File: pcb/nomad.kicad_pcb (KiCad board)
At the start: 2 copper layers, 61 x 142 mm, 65 parts, among them J1 USB_C_Receptacle_USB2.0_16P, J2 Conn_01x08_Pin, J3 Conn_Coaxial, J4 Conn_Coaxial, J5 Conn_01x02_Pin, Q2 2N7002, SW1 UP, SW2 DOWN, SW3 RIGHT, SW4 LEFT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

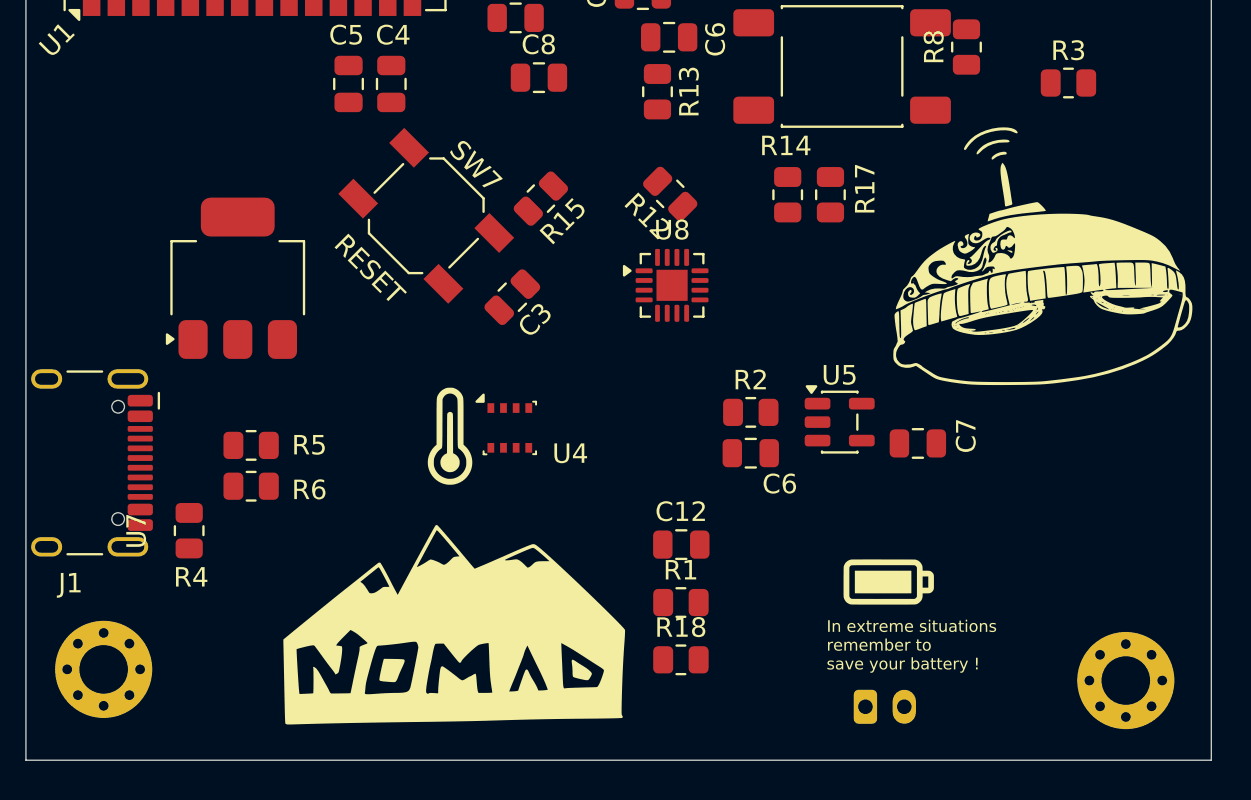
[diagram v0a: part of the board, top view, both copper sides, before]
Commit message: Updating PCB: Adding Buck boost converter, battery protection and other fixes.
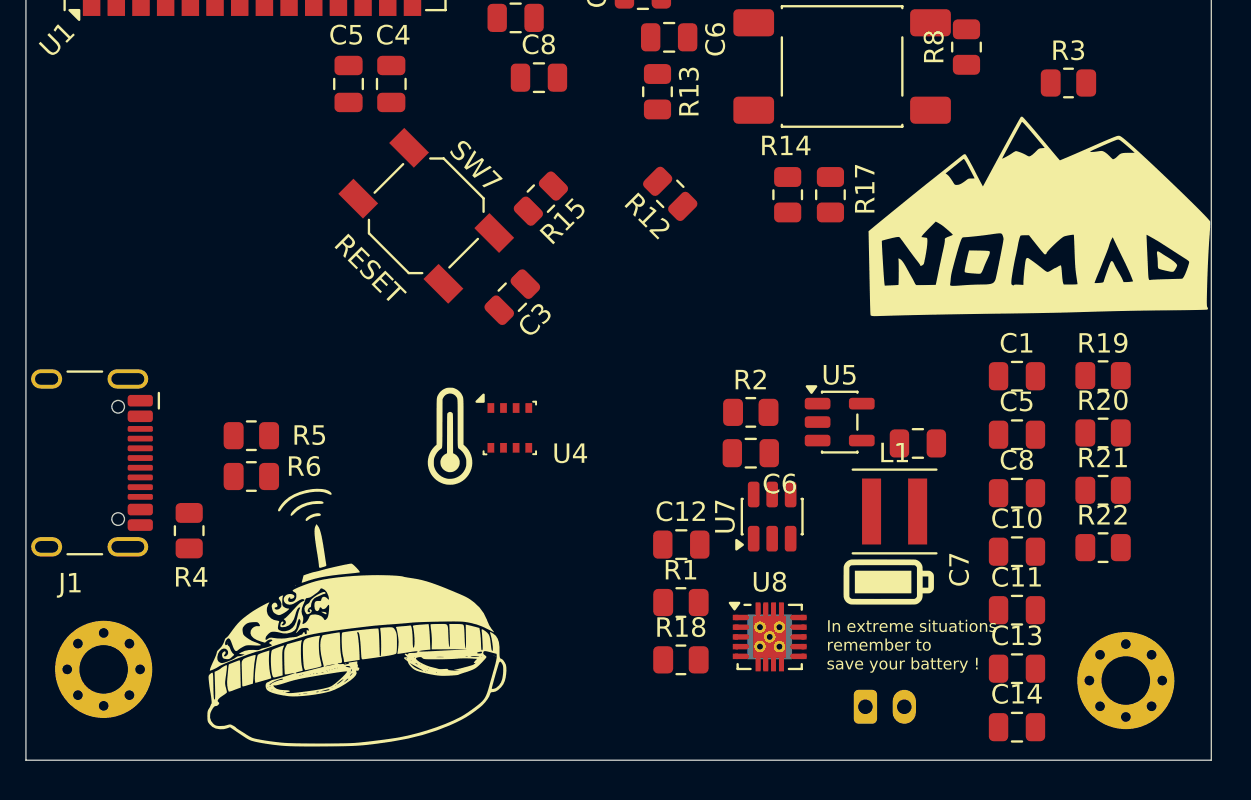
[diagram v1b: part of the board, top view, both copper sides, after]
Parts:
- added C1: C, Capacitor_SMD:C_0805_2012Metric, F.Cu at (151.0, 142.2)
- added C10: C, Capacitor_SMD:C_0805_2012Metric, F.Cu at (151.0, 151.3)
- added C11: C, Capacitor_SMD:C_0805_2012Metric, F.Cu at (151.0, 154.3)
- added C13: 10uF, Capacitor_SMD:C_0805_2012Metric, F.Cu at (151.0, 157.3)
- added C14: 66uF, Capacitor_SMD:C_0805_2012Metric, F.Cu at (151.0, 160.3)
- added C5: 22uF, Capacitor_SMD:C_0805_2012Metric, F.Cu at (151.0, 145.2)
- added C8: 0.1uF, Capacitor_SMD:C_0805_2012Metric, F.Cu at (151.0, 148.3)
- added L1: 1uH, Inductor_SMD:L_Coilcraft_XxL4020, F.Cu at (144.7, 149.2)
- added R19: 100R, Resistor_SMD:R_0805_2012Metric, F.Cu at (155.4, 142.2)
- added R20: 560k, Resistor_SMD:R_0805_2012Metric, F.Cu at (155.4, 145.2)
- added R21: 1M, Resistor_SMD:R_0805_2012Metric, F.Cu at (155.4, 148.1)
- added R22: 100k, Resistor_SMD:R_0805_2012Metric, F.Cu at (155.4, 151.1)
- U7: value AMS1117-3.3 -> DW01A; footprint Package_TO_SOT_SMD:SOT-223-3_TabPin2 -> Package_TO_SOT_SMD:SOT-23-6
- U8: value BQ24075RGT -> TPS63060; footprint Package_DFN_QFN:VQFN-16-1EP_3x3mm_P0.5mm_EP1.6x1.6mm -> Package_SON:Texas_S-PWSON-N10_ThermalVias
- moved G*** 39.9 mm to (131.2, 202.3)
- moved G*** 36.7 mm to (152.2, 134.1)
- moved U7 30.1 mm to (138.4, 149.5)
- moved U8 18.8 mm to (138.3, 155.7)
- moved R5 0.50 mm to (111.6, 145.3)
- moved R6 0.50 mm to (111.6, 147.4)
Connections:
- C6 pad 1: Net-(J5-Pin_1) -> +BATT
- J2 pad 5: SDA -> MOSI
- J2 pad 6: SCL -> SCLK
- J5 pad 1: Net-(J5-Pin_1) -> +BATT
- J5 pad 2: GND -> -BATT
- U1 pad 18: unconnected-(U1-IO10-Pad18) -> CS
- U1 pad 19: unconnected-(U1-IO11-Pad19) -> MOSI
- U1 pad 20: unconnected-(U1-IO12-Pad20) -> SCLK
- U1 pad 25: unconnected-(U1-IO48-Pad25) -> M1
- U1 pad 31: unconnected-(U1-IO38-Pad31) -> M0
- U1 pad 38: unconnected-(U1-IO2-Pad38) -> BUTTON_INT
- U1 pad 39: unconnected-(U1-IO1-Pad39) -> FLASHLIGHT
- U1 pad 6: unconnected-(U1-IO6-Pad6) -> RES
- U1 pad 7: unconnected-(U1-IO7-Pad7) -> DC
- U5 pad 3: Net-(J5-Pin_1) -> +BATT
- U7 pad 1: GND -> unconnected-(U7-OD-Pad1)
- U7 pad 2: +3V3 -> unconnected-(U7-CS-Pad2)
- U7 pad 3: +5V -> unconnected-(U7-OC-Pad3)
- U8 pad 1: unconnected-(U8-TS-Pad1) -> Net-(U8-L1)
- U8 pad 10: Net-(U8-OUT-Pad10) -> Net-(U8-L2)
- U8 pad 11: Net-(U8-OUT-Pad10) -> GND
- U8 pad 2: Net-(U8-BAT-Pad2) -> +BATT
- U8 pad 3: Net-(U8-BAT-Pad2) -> +BATT
- U8 pad 4: unconnected-(U8-~{CE}-Pad4) -> GND
- U8 pad 5: unconnected-(U8-EN2-Pad5) -> Net-(U8-PG)
- U8 pad 6: unconnected-(U8-EN1-Pad6) -> Net-(U8-VAUX)
- U8 pad 7: unconnected-(U8-~{PGOOD}-Pad7) -> GND
- U8 pad 8: Net-(U8-VSS-Pad17) -> Net-(U8-FB)
- U8 pad 9: unconnected-(U8-~{CHG}-Pad9) -> Net-(U8-VOUT)
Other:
- board text added: "USB-C > charging IC > JST > MAX > Buck boost"

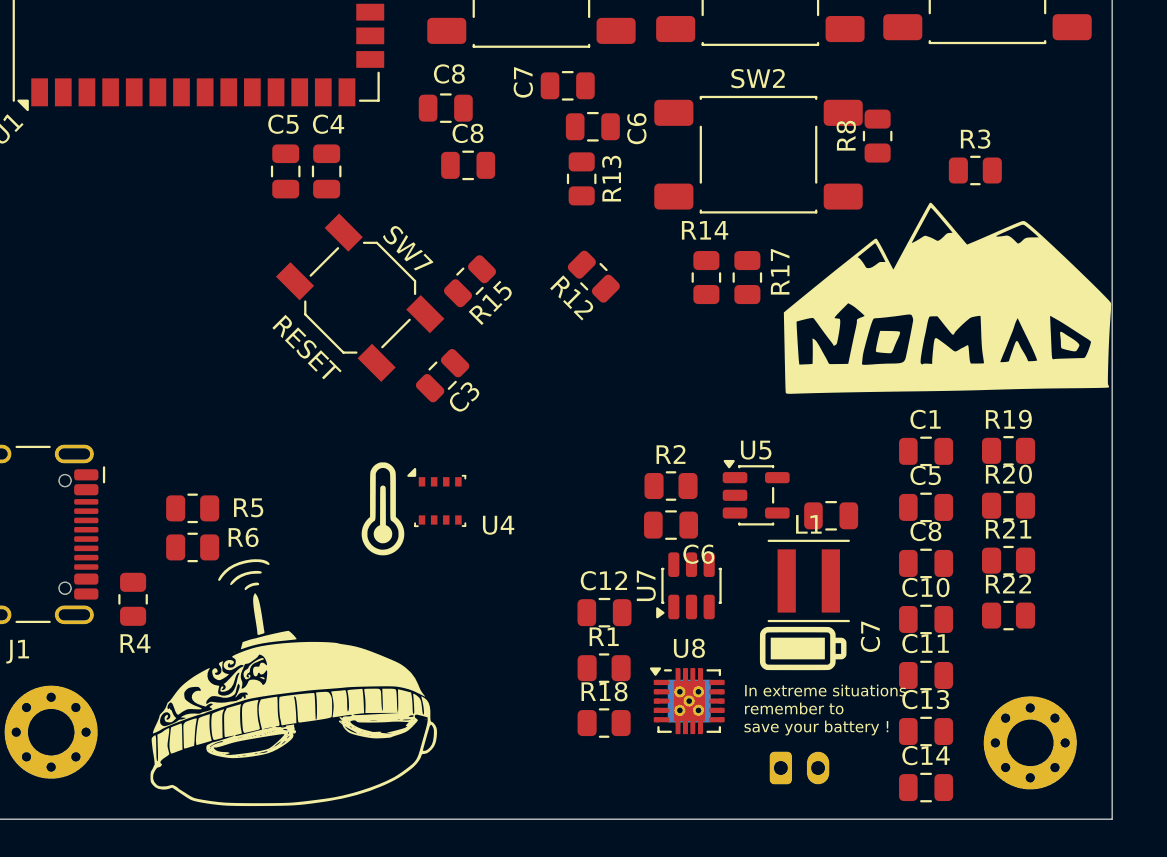
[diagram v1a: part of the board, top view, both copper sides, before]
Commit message: Updating PCB: Removing battery security and adding slide switch
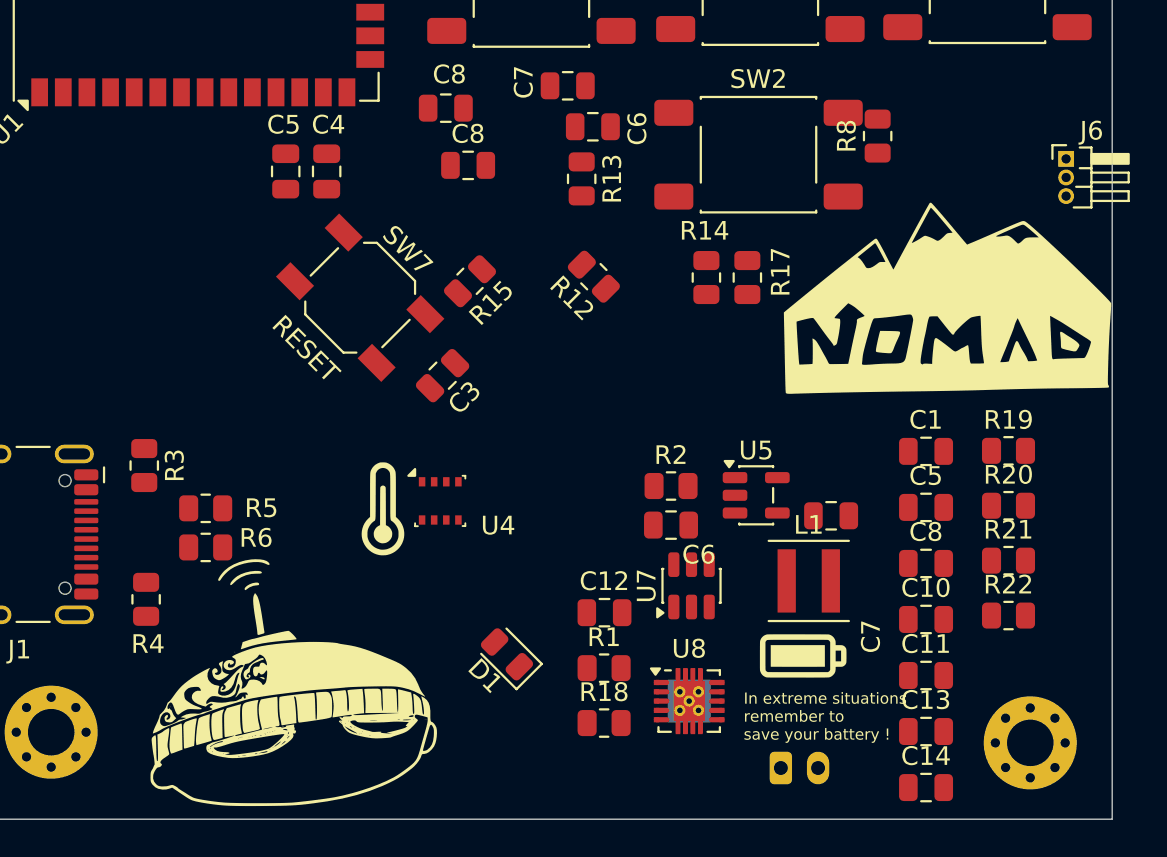
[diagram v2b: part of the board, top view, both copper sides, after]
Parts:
- added D1: LED, LED_SMD:LED_0805_2012Metric, F.Cu at (128.5, 153.1)
- added J6: Conn_01x03_Socket, Connector_PinHeader_1.00mm:PinHeader_1x03_P1.00mm_Horizontal, F.Cu at (158.5, 126.5)
- moved R3 47.4 mm to (109.0, 143.0), turned to -90 degrees
- moved R5 0.70 mm to (112.3, 145.3)
- moved R6 0.70 mm to (112.3, 147.4)
- moved R4 0.70 mm to (109.1, 150.2)
- moved G*** 0.40 mm to (144.4, 153.2)
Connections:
- C5 pad 2: +BATT -> SWBAT+
- U8 pad 2: +BATT -> SWBAT+
- U8 pad 3: +BATT -> SWBAT+
